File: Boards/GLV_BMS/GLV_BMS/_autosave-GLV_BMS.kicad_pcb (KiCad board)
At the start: 2 copper layers, 44 parts, among them J1 CONN_02X03, J2 CONN_02X03, J3 MM_F_RA_20, U1 MCP2561-E_SN, U101 TPS560430YF, U2 ATMEGA16M1, U3 ATmega328P-AU, Y1 Crystal_SMD, Y2 Crystal_SMD

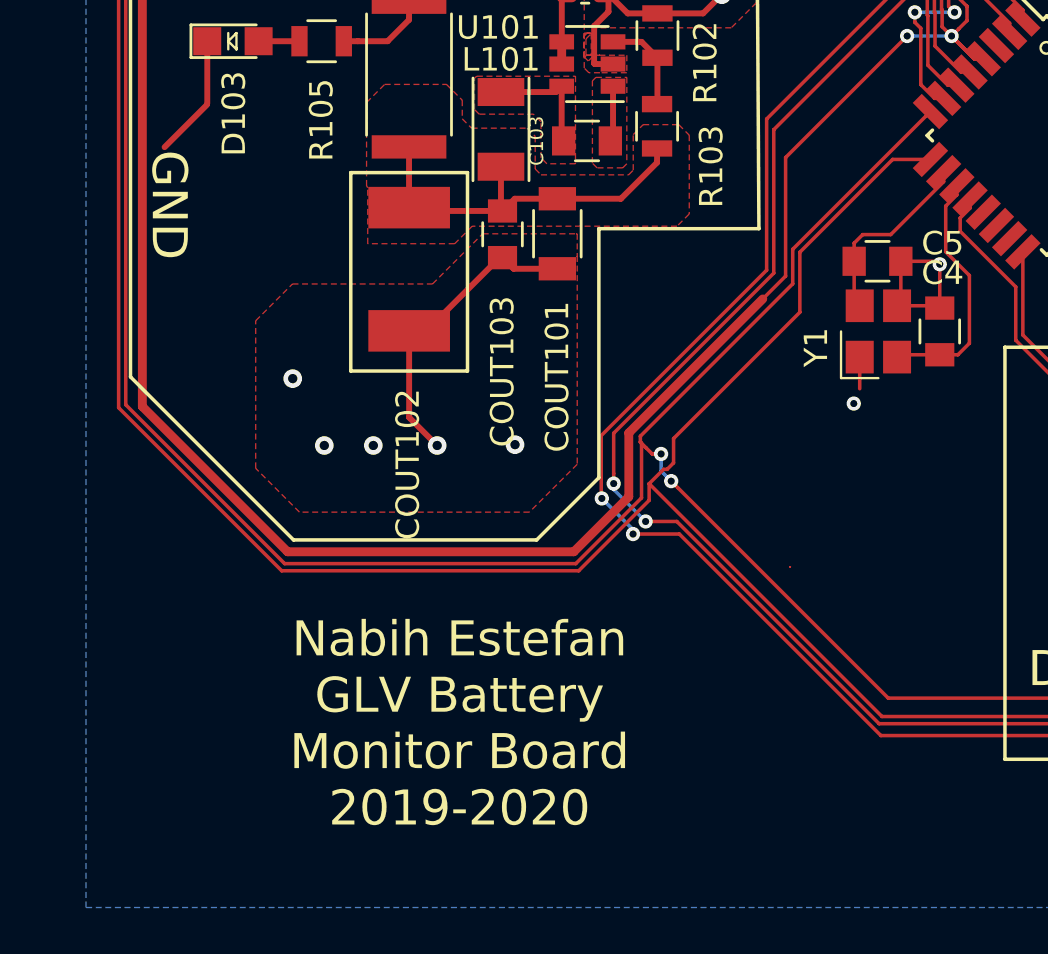
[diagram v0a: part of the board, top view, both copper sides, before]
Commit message: created BOM for board
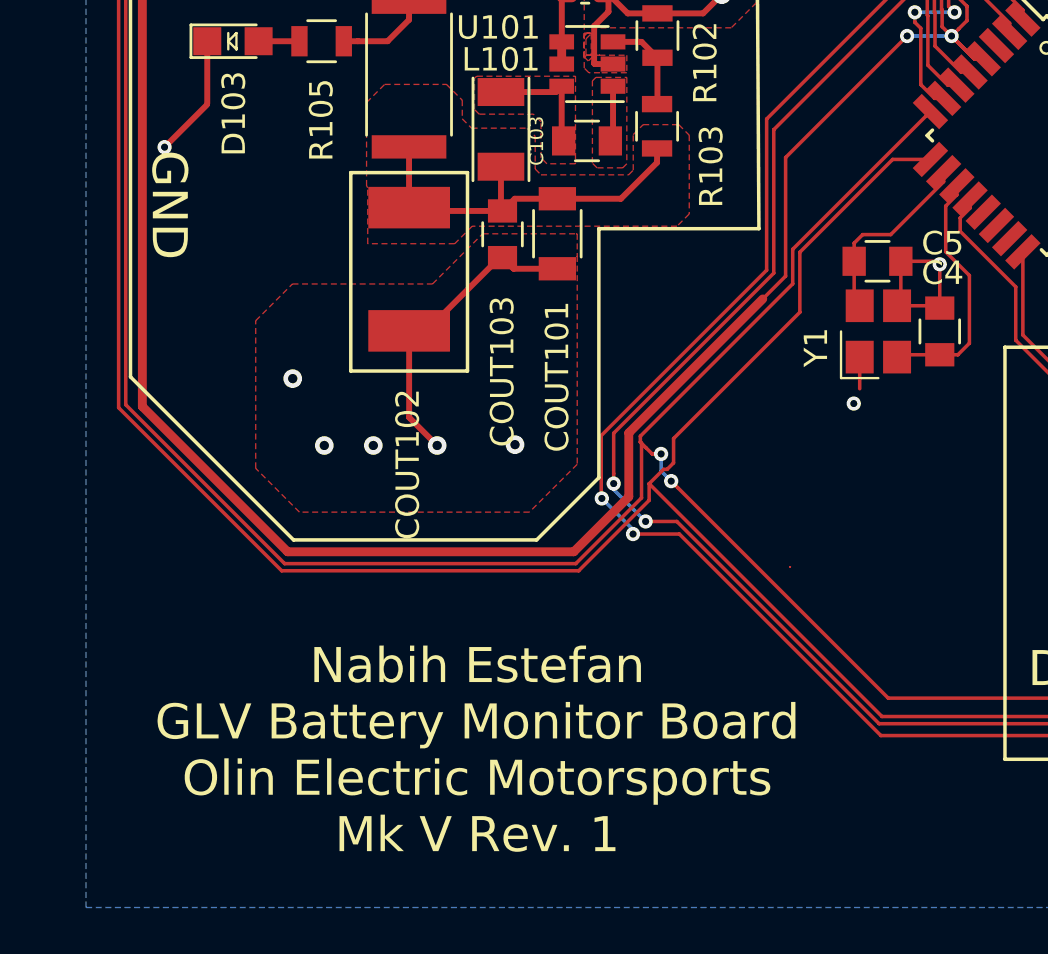
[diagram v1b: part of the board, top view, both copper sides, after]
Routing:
- net GND: vias 24 -> 25
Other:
- board text added: "Nabih Estefan GLV Battery Monitor Board Olin Electric Motorsports Mk V Rev. 1"
- board text removed: "Nabih Estefan GLV Battery Monitor Board 2019-2020"
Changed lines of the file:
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@@
     (thickness 1.6)
     (drawings 50)
-    (tracks 782)
+    (tracks 784)
     (zones 0)
     (modules 44)
@@
   (gr_line (start 185.42 74.93) (end 186.499999 74.93) (layer Dwgs.User) (width 0.2))
   (gr_line (start 185.42 74.93) (end 185.42 71.12) (layer Dwgs.User) (width 0.2))
-  (gr_text "Nabih Estefan\nGLV Battery\nMonitor Board\n2019-2020\n" (at 115.062 128.016) (layer F.SilkS)
+  (gr_text "Nabih Estefan\nGLV Battery Monitor Board\nOlin Electric Motorsports\nMk V Rev. 1\n" (at 115.824 129.159) (layer F.SilkS)
     (effects (font (size 1.5 1.5) (thickness 0.3)))
   )
@@
   (segment (start 135.407378 97.534492) (end 135.407378 95.148378) (width 0.1524) (layer F.Cu) (net 1))
   (segment (start 135.407378 95.148378) (end 134.347934 94.088934) (width 0.1524) (layer F.Cu) (net 1))
+  (segment (start 102.4255 103.3145) (end 102.4255 103.3145) (width 0.254) (layer F.Cu) (net 1))
+  (via (at 102.4255 103.3145) (size 0.6096) (drill 0.3048) (layers F.Cu B.Cu) (net 1))
   (segment (start 112.89792 97.1042) (end 112.89792 97.8582) (width 0.254) (layer F.Cu) (net 2))
   (segment (start 112.89792 97.8582) (end 111.98012 98.776) (width 0.254) (layer F.Cu) (net 2))
@@
     (connect_pads yes (clearance 0.1524))
     (min_thickness 0.1524)
-    (fill (arc_segments 16) (thermal_gap 0.508) (thermal_bridge_width 0.508))
+    (fill yes (arc_segments 16) (thermal_gap 0.508) (thermal_bridge_width 0.508))
     (polygon
       (pts
@@
     (connect_pads yes (clearance 0.1524))
     (min_thickness 0.1524)
-    (fill (arc_segments 16) (thermal_gap 0.508) (thermal_bridge_width 0.508))
+    (fill yes (arc_segments 16) (thermal_gap 0.508) (thermal_bridge_width 0.508))
     (polygon
       (pts
@@
     (connect_pads yes (clearance 0.1524))
     (min_thickness 0.1524)
-    (fill (arc_segments 16) (thermal_gap 0.508) (thermal_bridge_width 0.508))
+    (fill yes (arc_segments 16) (thermal_gap 0.508) (thermal_bridge_width 0.508))
     (polygon
       (pts
@@
     (connect_pads yes (clearance 0.1524))
     (min_thickness 0.1524)
-    (fill (arc_segments 16) (thermal_gap 0.508) (thermal_bridge_width 0.508))
+    (fill yes (arc_segments 16) (thermal_gap 0.508) (thermal_bridge_width 0.508))
     (polygon
       (pts
@@
     (connect_pads yes (clearance 0.1524))
     (min_thickness 0.1524)
-    (fill (arc_segments 16) (thermal_gap 0.508) (thermal_bridge_width 0.508))
+    (fill yes (arc_segments 16) (thermal_gap 0.508) (thermal_bridge_width 0.508))
     (polygon
       (pts
@@
     (connect_pads yes (clearance 0.1524))
     (min_thickness 0.1524)
-    (fill (arc_segments 16) (thermal_gap 0.508) (thermal_bridge_width 0.508))
+    (fill yes (arc_segments 16) (thermal_gap 0.508) (thermal_bridge_width 0.508))
     (polygon
       (pts
@@
     (connect_pads yes (clearance 0.1524))
     (min_thickness 0.1524)
-    (fill (arc_segments 16) (thermal_gap 0.508) (thermal_bridge_width 0.508))
+    (fill yes (arc_segments 16) (thermal_gap 0.508) (thermal_bridge_width 0.508))
     (polygon
       (pts
@@
     (connect_pads yes (clearance 0.1524))
     (min_thickness 0.254)
-    (fill (arc_segments 16) (thermal_gap 0.508) (thermal_bridge_width 0.508))
+    (fill yes (arc_segments 16) (thermal_gap 0.508) (thermal_bridge_width 0.508))
     (polygon
       (pts
@@
     (connect_pads yes (clearance 0.1524))
     (min_thickness 0.1524)
-    (fill (arc_segments 16) (thermal_gap 0.508) (thermal_bridge_width 0.508))
+    (fill yes (arc_segments 16) (thermal_gap 0.508) (thermal_bridge_width 0.508))
     (polygon
       (pts
